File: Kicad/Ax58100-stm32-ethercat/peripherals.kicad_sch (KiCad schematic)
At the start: 18 parts, among them J14 I2C bus2, J2 Encoder 1, J4 Encoder 2, J6 Encoder 4, J7 DAC1, J8 Encoder 3

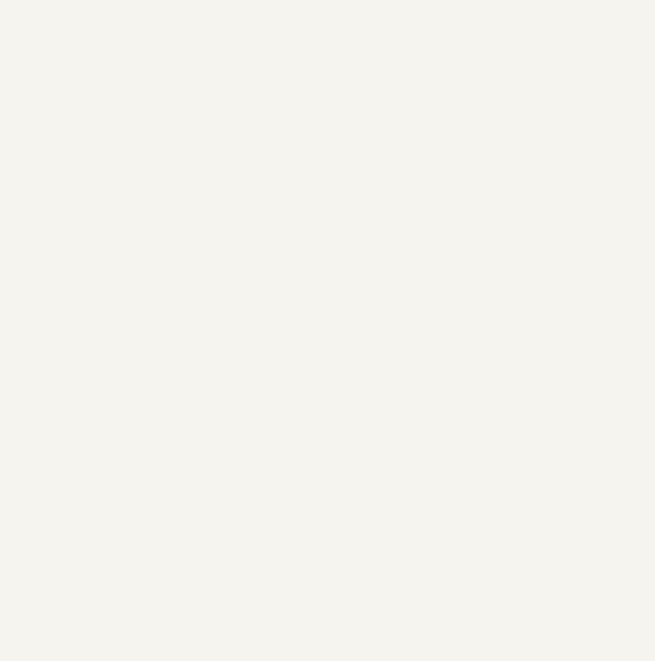
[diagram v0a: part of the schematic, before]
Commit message: Added optional pull-down to step generators
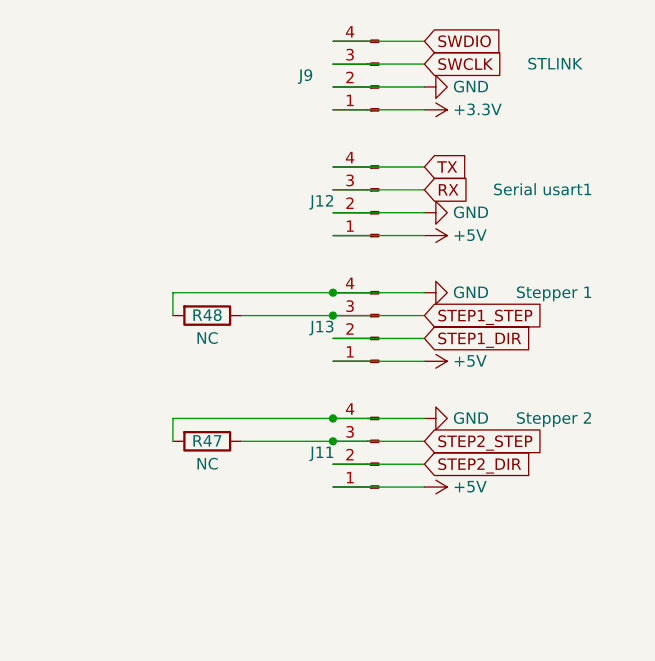
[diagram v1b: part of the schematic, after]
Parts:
- added J11: Stepper 2, Connector_JST:JST_XH_B4B-XH-A_1x04_P2.50mm_Vertical, symbol Connector:Conn_01x04_Pin
- added J12: Serial usart1, Connector_JST:JST_XH_B4B-XH-A_1x04_P2.50mm_Vertical, symbol Connector:Conn_01x04_Pin
- added J13: Stepper 1, Connector_JST:JST_XH_B4B-XH-A_1x04_P2.50mm_Vertical, symbol Connector:Conn_01x04_Pin
- added J9: STLINK, Connector_JST:JST_XH_B4B-XH-A_1x04_P2.50mm_Vertical, symbol Connector:Conn_01x04_Pin
- added R47, R48: NC, Resistor_SMD:R_0805_2012Metric, symbol Device:R
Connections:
- net +3.3V: now also J9.1 (Pin_1)
- net +5V: now also J11.1 (Pin_1), J12.1 (Pin_1), J13.1 (Pin_1)
- net GND: now also J11.4 (Pin_4), J12.2 (Pin_2), J13.4 (Pin_4), J9.2 (Pin_2), R47.2, R48.2
- new net RX: J12.3 (Pin_3)
- new net STEP1_DIR: J13.2 (Pin_2)
- new net STEP1_STEP: J13.3 (Pin_3), R48.1
- new net STEP2_DIR: J11.2 (Pin_2)
- new net STEP2_STEP: J11.3 (Pin_3), R47.1
- new net SWCLK: J9.3 (Pin_3)
- new net SWDIO: J9.4 (Pin_4)
- new net TX: J12.4 (Pin_4)

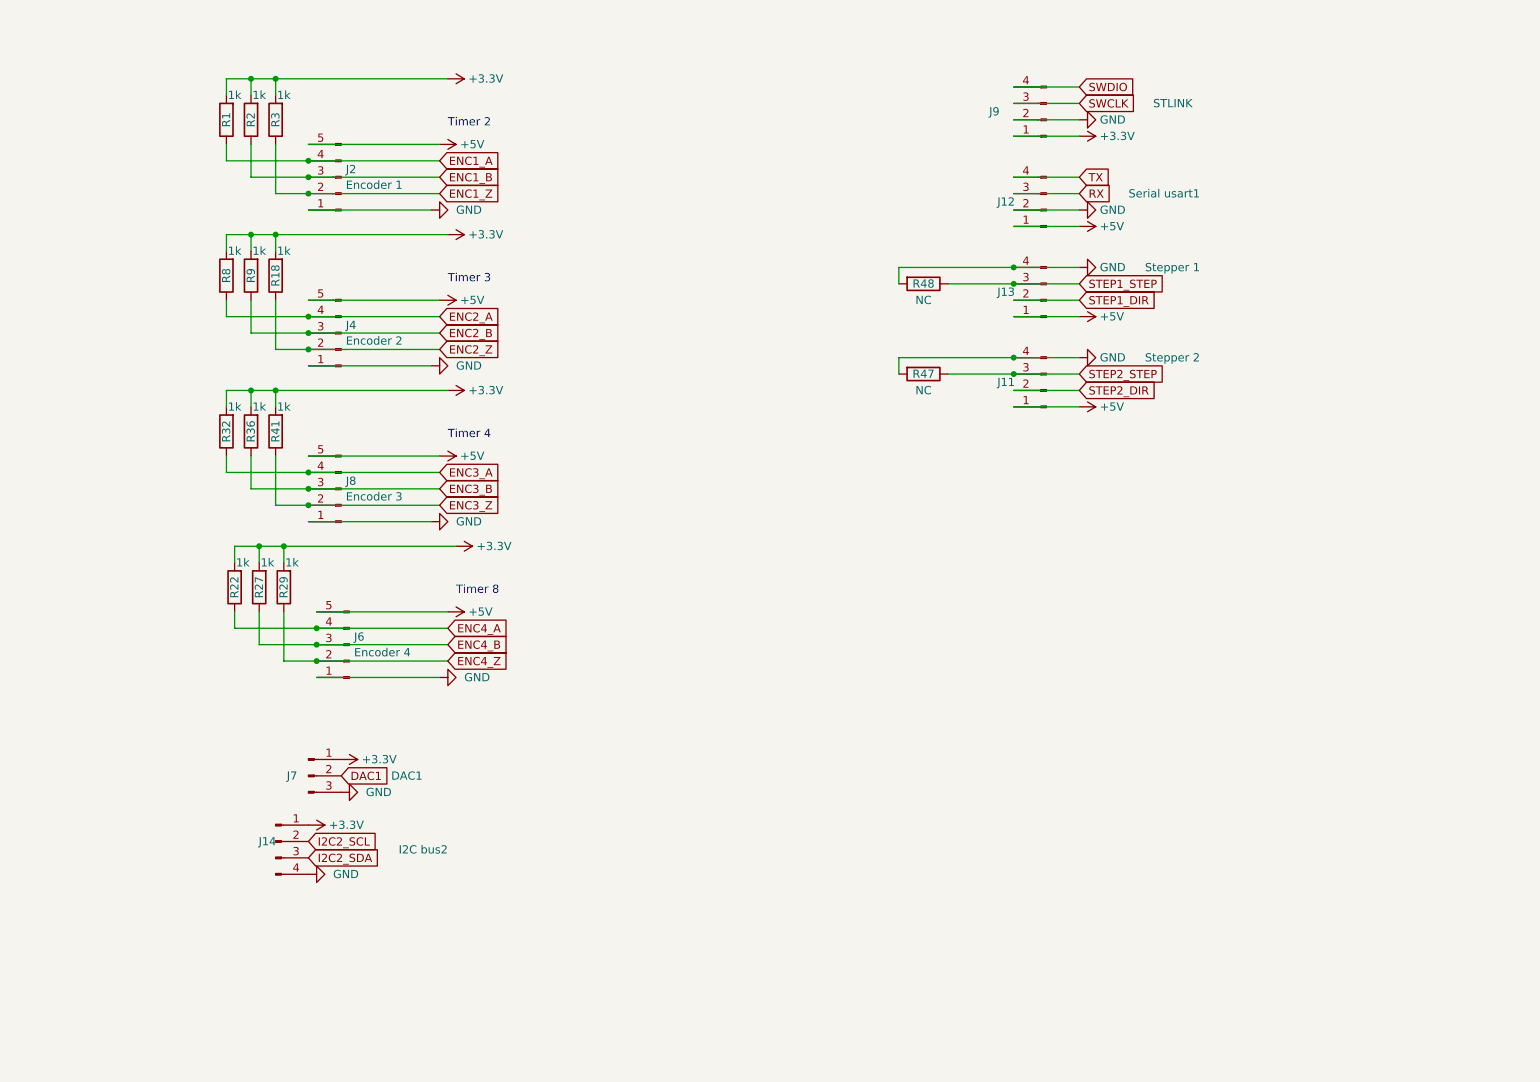
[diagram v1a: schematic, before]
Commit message: wip inputs with photodiodes etc
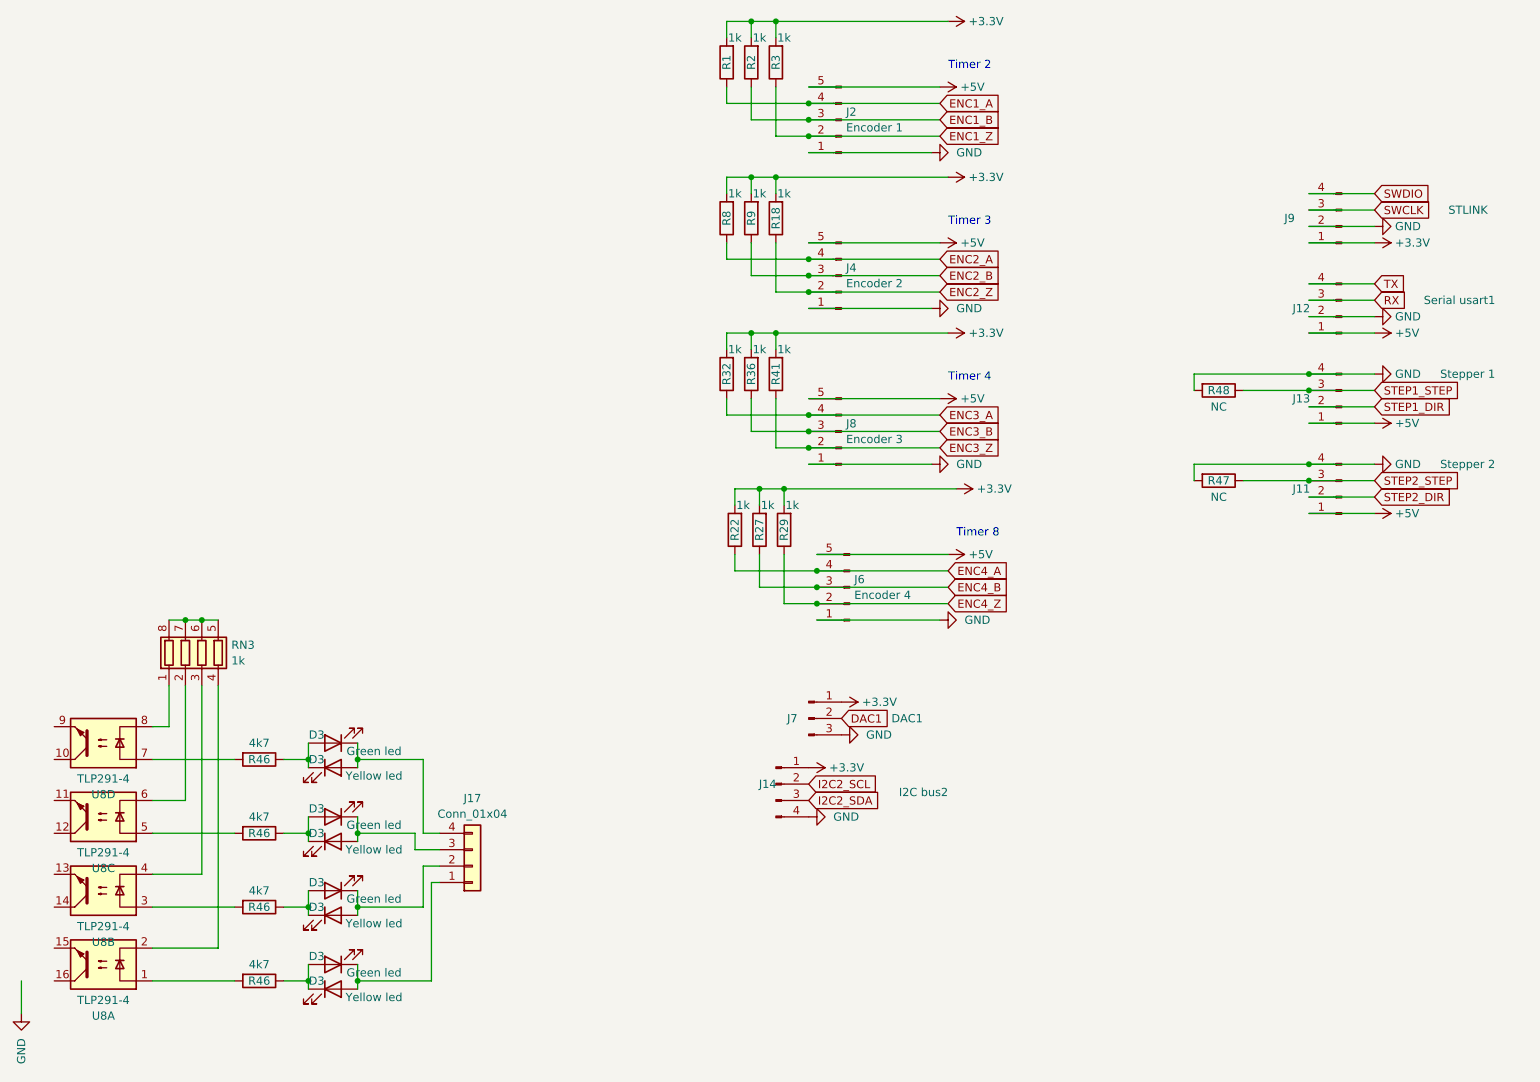
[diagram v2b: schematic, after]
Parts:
- added D3 (x4): Yellow led, LED_SMD:LED_0805_2012Metric, symbol Device:LED
- added D3 (x4): Green led, LED_SMD:LED_0805_2012Metric, symbol Device:LED
- added J17: Conn_01x04, symbol Connector_Generic:Conn_01x04
- added R46 (x4): 4k7, Resistor_SMD:R_1210_3225Metric, symbol Device:R
- added RN3: 1k, symbol Device:R_Pack04
- added U8: TLP291-4, Package_SO:SOIC-16_4.55x10.3mm_P1.27mm, symbol Isolator:TLP291-4
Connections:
- new net: D3.1 (K), D3.2 (A), R46.1 (x4)
- new net: D3.1 (K), D3.2 (A), J17.3 (Pin_3)
- new net: D3.1 (K), D3.2 (A), J17.2 (Pin_2)
- new net: RN3.1 (R1.1), U8.8
- new net: RN3.2 (R2.1), U8.6
- new net: RN3.3 (R3.1), U8.4
- new net: RN3.4 (R4.1), U8.2
- new net: RN3.5 (R4.2), RN3.6 (R3.2), RN3.7 (R2.2), RN3.8 (R1.2)
- new net: R46.2, U8.7
- new net: R46.2, U8.1
- new net: D3.1 (K), D3.2 (A), J17.1 (Pin_1)
- new net: D3.1 (K), D3.2 (A), J17.4 (Pin_4)
- new net: R46.2, U8.5
- new net: R46.2, U8.3
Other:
- moved on the sheet: J11, J12, J13, J14, J2, J4, J6, J7, J8, J9, R1, R18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

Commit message: Wip optocoupler input and outputs
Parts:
- added D3 (x4): Yellow led, LED_SMD:LED_0805_2012Metric, symbol Device:LED
- added D3 (x4): Green led, LED_SMD:LED_0805_2012Metric, symbol Device:LED
- added J15: Conn_01x04, symbol Connector_Generic:Conn_01x04
- added J16: Conn_01x02, symbol Connector_Generic:Conn_01x02
- added J18: Conn_01x08, symbol Connector_Generic:Conn_01x08
- added R46 (x4): 4k7, Resistor_SMD:R_1210_3225Metric, symbol Device:R
- added RN1, RN2, RN4, RN5: 1k, symbol Device:R_Pack04
- added U6, U7: TLP291-4, Package_SO:SOIC-16_4.55x10.3mm_P1.27mm, symbol Isolator:TLP291-4
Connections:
- net +3.3V: now also U8.10, U8.12, U8.14, U8.16, U6.10, U6.12, U6.14, U6.16
- net GND: now also RN1.5 (R4.2), RN1.6 (R3.2), RN1.7 (R2.2), RN1.8 (R1.2), RN2.5 (R4.2), RN2.6 (R3.2), RN2.7 (R2.2), RN2.8 (R1.2), RN5.5 (R4.2), RN5.6 (R3.2), RN5.7 (R2.2), RN5.8 (R1.2)
- net -24V_FIELD: now reaches RN3.5 (R4.2), RN3.6 (R3.2), RN3.7 (R2.2), RN3.8 (R1.2)
- net -24V_FIELD: now also J16.1 (Pin_1), RN4.5 (R4.2), RN4.6 (R3.2), RN4.7 (R2.2), RN4.8 (R1.2)
- net IO9: now reaches U8.15
- net IO9: now also RN2.1 (R1.1)
- net IO12: now reaches U8.9
- net IO12: now also RN2.4 (R4.1)
- net IO11: now reaches U8.11
- net IO11: now also RN2.3 (R3.1)
- net IO10: now reaches U8.13
- net IO10: now also RN2.2 (R2.1)
- new net: R46.2, U6.3
- new net: RN4.3 (R3.1), U6.4
- new net: D3.1 (K), D3.2 (A), R46.1 (x4)
- new net: R46.2, U6.1
- new net: R46.2, U6.7
- new net: J18.7 (Pin_7), U7.10
- new net: RN5.4 (R4.1), U7.8
- new net: J18.8 (Pin_8), U7.9
- new net: RN4.1 (R1.1), U6.8
- new net: J18.2 (Pin_2), U7.15
- new net: J18.1 (Pin_1), U7.16
- new net: RN5.1 (R1.1), U7.2
- new net: D3.1 (K), D3.2 (A), J15.1 (Pin_1)
- new net: D3.1 (K), D3.2 (A), J15.2 (Pin_2)
- new net: D3.1 (K), D3.2 (A), J15.3 (Pin_3)
- new net: D3.1 (K), D3.2 (A), J15.4 (Pin_4)
- new net: RN4.4 (R4.1), U6.2
- new net: RN5.2 (R2.1), U7.4
- new net: RN5.3 (R3.1), U7.6
- new net: R46.2, U6.5
- new net: RN4.2 (R2.1), U6.6
- new net: J18.3 (Pin_3), U7.14
- new net: J18.4 (Pin_4), U7.13
- new net: J18.5 (Pin_5), U7.12
- new net: J18.6 (Pin_6), U7.11
- new net +24V_FIELD: J16.2 (Pin_2)
- new net IO1: U7.1
- new net IO2: U7.3
- new net IO3: U7.5
- new net IO4: U7.7
- new net IO5: RN1.1 (R1.1), U6.15
- new net IO6: RN1.2 (R2.1), U6.13
- new net IO7: RN1.3 (R3.1), U6.11
- new net IO8: RN1.4 (R4.1), U6.9
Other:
- note added: "Inputs"
- note added: "Outputs"
- moved on the sheet: D3, J11, J12, J13, J14, J17, J2, J4, J6, J7, J8, J9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

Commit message: Steppers, encoders, IO, etc remapped
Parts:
- removed D3 (x8): Green led, LED_SMD:LED_0805_2012Metric, symbol Device:LED
- removed J11: Stepper 2, Connector_JST:JST_XH_B4B-XH-A_1x04_P2.50mm_Vertical, symbol Connector:Conn_01x04_Pin
- removed J12: Serial usart1, Connector_JST:JST_XH_B4B-XH-A_1x04_P2.50mm_Vertical, symbol Connector:Conn_01x04_Pin
- removed J13: Stepper 1, Connector_JST:JST_XH_B4B-XH-A_1x04_P2.50mm_Vertical, symbol Connector:Conn_01x04_Pin
- removed J14: I2C bus2, Connector_PinHeader_2.54mm:PinHeader_1x04_P2.54mm_Vertical, symbol Connector:Conn_01x04_Pin
- removed J2: Encoder 1, Connector_JST:JST_XH_B5B-XH-A_1x05_P2.50mm_Vertical, symbol Connector:Conn_01x05_Pin
- removed J4: Encoder 2, Connector_JST:JST_XH_B5B-XH-A_1x05_P2.50mm_Vertical, symbol Connector:Conn_01x05_Pin
- removed J6: Encoder 4, Connector_JST:JST_XH_B5B-XH-A_1x05_P2.50mm_Vertical, symbol Connector:Conn_01x05_Pin
- removed J7: DAC1, Connector_JST:JST_XH_B3B-XH-A_1x03_P2.50mm_Vertical, symbol Connector:Conn_01x03_Pin
- removed J8: Encoder 3, Connector_JST:JST_XH_B5B-XH-A_1x05_P2.50mm_Vertical, symbol Connector:Conn_01x05_Pin
- removed J9: STLINK, Connector_JST:JST_XH_B4B-XH-A_1x04_P2.50mm_Vertical, symbol Connector:Conn_01x04_Pin
- removed R1, R18, R2, R22, R27, R29, R3, R32, R36, R41, R8, R9: 1k, Resistor_SMD:R_0805_2012Metric, symbol Device:R
- removed R47, R48: NC, Resistor_SMD:R_0805_2012Metric, symbol Device:R
- added J1: Out_opt, symbol Connector_Generic:Conn_01x06
- added J3: In_opt1, symbol Connector_Generic:Conn_01x06
- added J5: In_opt2, symbol Connector_Generic:Conn_01x06
- added J6: DAC, symbol Connector_Generic:Conn_01x03
- U6, U8: value TLP291-4 -> TLP292-4
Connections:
- net +3.3V: now also J6.1 (Pin_1)
- net +5V: now also J1.1 (Pin_1), J3.1 (Pin_1), J5.1 (Pin_1)
- net DAC1: now also J6.2 (Pin_2)
- net GND: now also J1.6 (Pin_6), J3.6 (Pin_6), J5.6 (Pin_6), J6.3 (Pin_3)
- net IO1: now also J1.2 (Pin_2)
- net IO10: now also J5.3 (Pin_3)
- net IO11: now also J5.4 (Pin_4)
- net IO12: now also J5.5 (Pin_5)
- net IO2: now also J1.3 (Pin_3)
- net IO3: now also J1.4 (Pin_4)
- net IO4: now also J1.5 (Pin_5)
- net IO5: now also J3.2 (Pin_2)
- net IO6: now also J3.3 (Pin_3)
- net IO7: now also J3.4 (Pin_4)
- net IO8: now also J3.5 (Pin_5)
- net IO9: now also J5.2 (Pin_2)
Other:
- note removed: "Timer 2"
- note removed: "Timer 3"
- note removed: "Timer 4"
- note removed: "Timer 8"
- title: (none) -> MetalMusings EaserCAT 3000
- moved on the sheet: D3, J18, RN5, U7A, U7B, U7C, U7D
